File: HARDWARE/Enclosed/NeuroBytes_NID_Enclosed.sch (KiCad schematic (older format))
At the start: 59 parts, among them J1 CONN_01X05, J2 Conn_01x03, J3 USB_OTG, J4 Conn_01x03_Female, J5 Conn_01x03, J6 Conn_01x03_Female, J7 Conn_01x03, J8 Conn_01x03_Female, Q1 MMBT3904, Q2 2N7002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

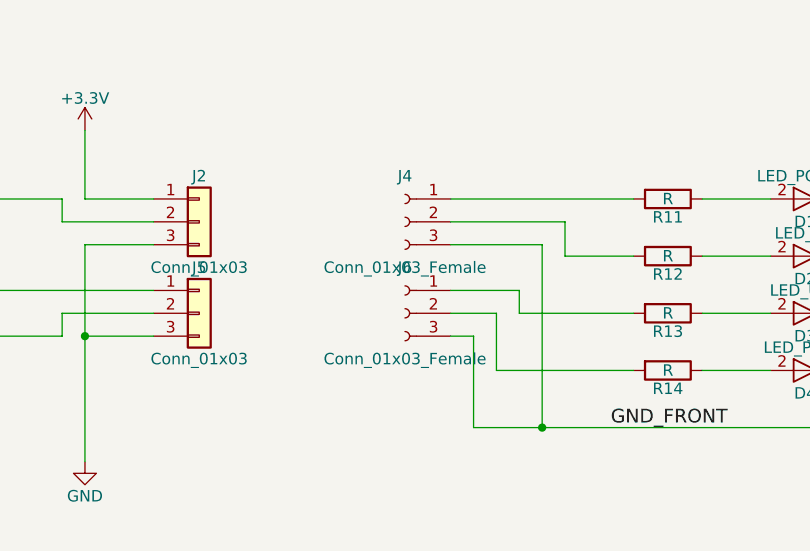
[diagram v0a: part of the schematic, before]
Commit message: assembled and tested board; fixed reversed traces on front panel. front-only files only include this board so they can be ordered alone.
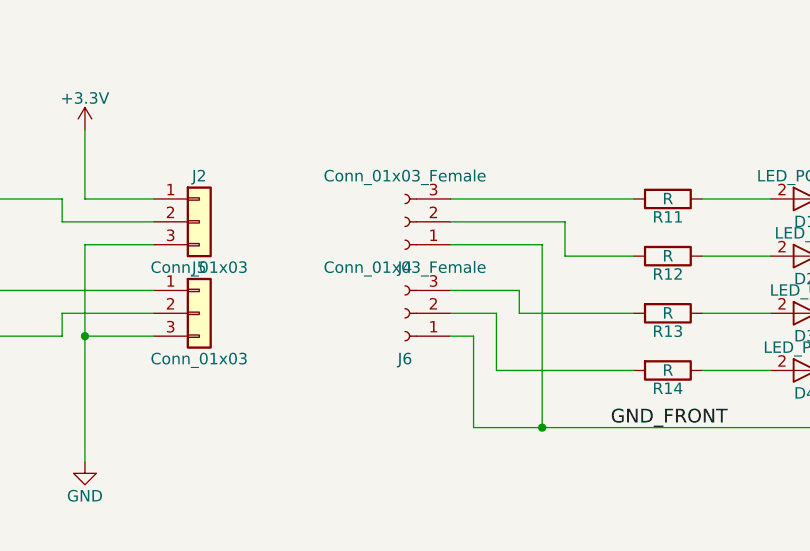
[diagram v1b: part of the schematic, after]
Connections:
- net GND_FRONT: now also J4.1 (Pin_1), J6.1 (Pin_1); no longer J4.3 (Pin_3), J6.3 (Pin_3)
- net at R11.2: now also J4.3 (Pin_3); no longer J4.1 (Pin_1)
- net at R13.2: now also J6.3 (Pin_3); no longer J6.1 (Pin_1)
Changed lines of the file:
@@
 F 5 "Yes" H 13700 1900 60  0001 C CNN "RoHS"
 	1    13700 1900
-	-1   0    0    -1
+	-1   0    0    1
 $EndComp
 Wire Wire Line
@@
 F 5 "Yes" H 13700 2300 60  0001 C CNN "RoHS"
 	1    13700 2300
-	-1   0    0    -1
+	-1   0    0    1
 $EndComp
 $Comp

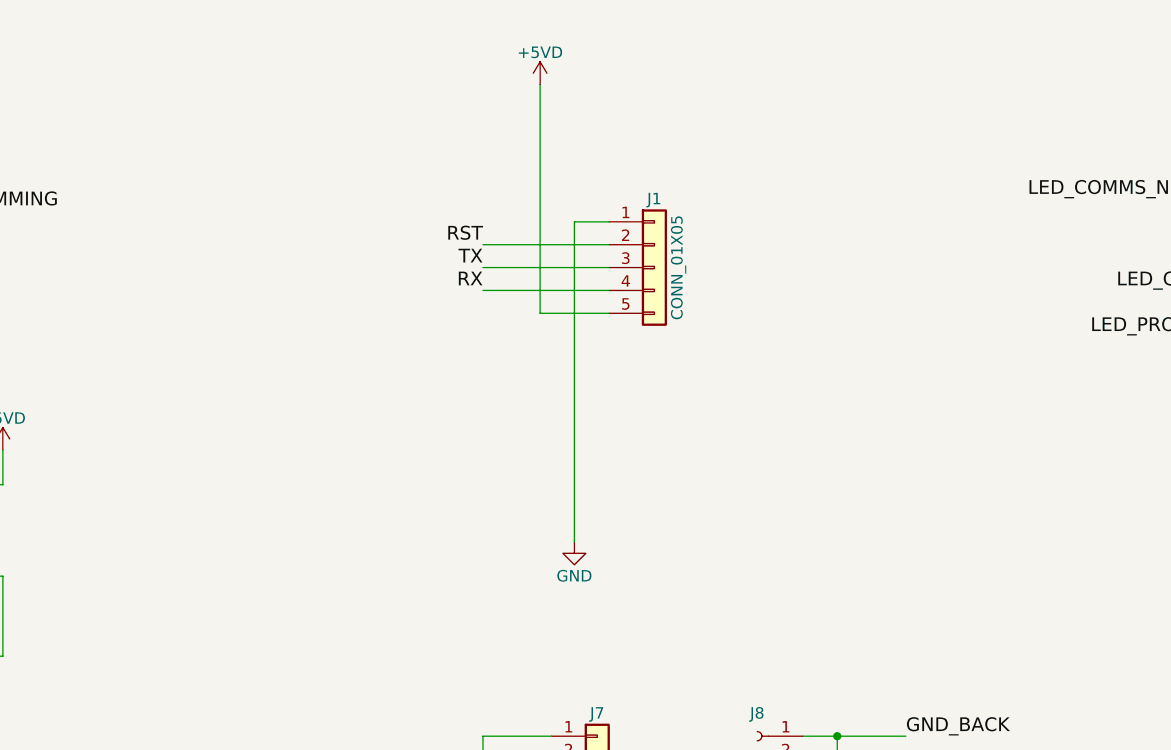
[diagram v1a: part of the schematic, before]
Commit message: added filtering to NeuroBytes network connection. updated USB ferrites and resonator footprints.
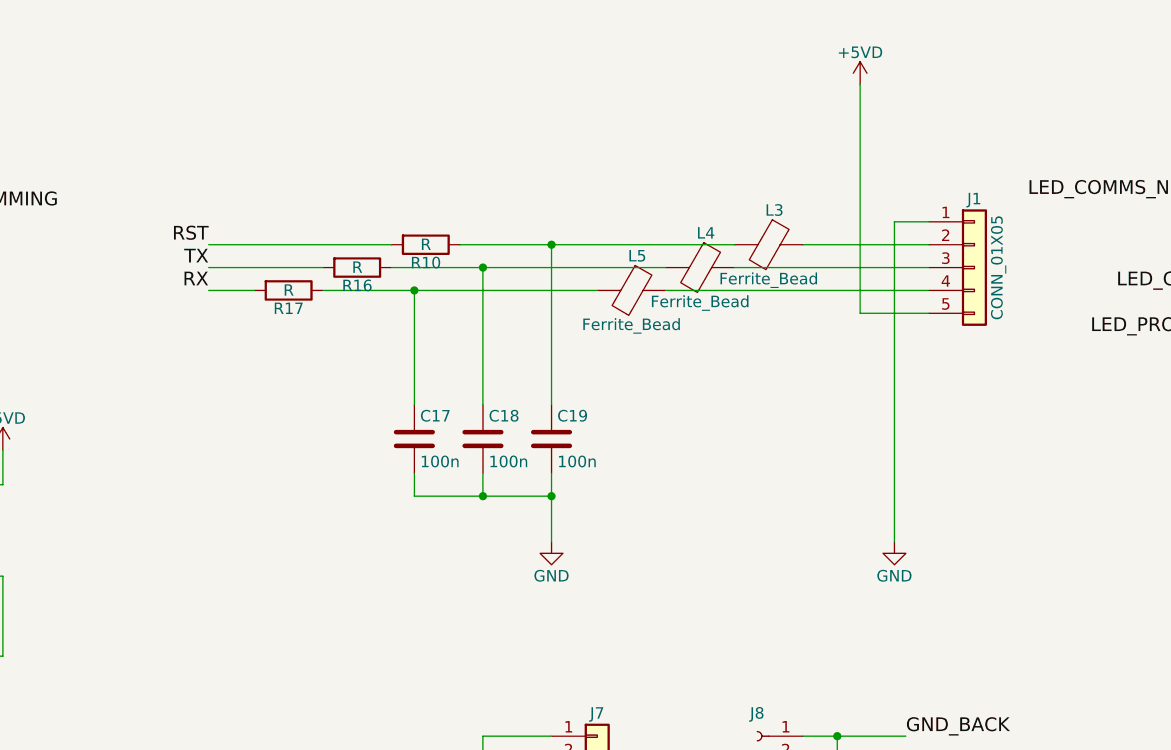
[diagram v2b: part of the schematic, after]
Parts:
- added C17, C18, C19: 100n, KiCad_Footprints:ZF_SMD_NonPol_0402_cap, symbol C
- added L3, L4, L5: Ferrite_Bead, KiCad_Footprints:ZF_SMD_NonPol_0603, symbol Ferrite_Bead
- added R10, R16, R17: R, KiCad_Footprints:ZF_SMD_NonPol_0402, symbol R
- Y1: footprint KiCad_Footprints:ZF_XTAL_PBRV_M -> KiCad_Footprints:ZF_XTAL_CSTCE_G; RoHS (none) -> Yes; Subs Allowed (none) -> No
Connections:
- net GND: now also C17.2, C18.2, C19.2
- net RST: now also R10.2; no longer J1.2 (Pin_2)
- net RX: now also R17.2; no longer J1.4 (Pin_4)
- net TX: now also R16.2; no longer J1.3 (Pin_3)
- new net: J1.2 (Pin_2), L3.1
- new net: J1.3 (Pin_3), L4.1
- new net: J1.4 (Pin_4), L5.1
- new net: C19.1, L3.2, R10.1
- new net: C18.1, L4.2, R16.1
- new net: C17.1, L5.2, R17.1
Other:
- moved on the sheet: J1
